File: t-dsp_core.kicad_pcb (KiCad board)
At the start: 4 copper layers, 100 x 61 mm, 164 parts, among them IC1 Logic Level Shifter - 74HCT2G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, J1 J_PWR, J10 J_DMX, J11 J_LED, J12 J_ETH, J13 u.FL DNP (IDC767 ext-antenna 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, J2 J_TDM, J3 J_T, J4 J_USBH, J5 J_MIDI, J6 J_SPDIF, J7 J_AUX, J8 J_S3, T108 Tab, T109 Tab, T110 Tab, T111 Tab, U1 Teensy 4.1 - DEVKIT, U11 Dual Buffer - SN74LVC2G125DCTR, U13 ESP32-S3-WROOM-1-N16R8, U15 LT3045EMSE#TRPBF, U16 THVD1450DR, U17 ISO7762DW, U18 TEA1-0505HI, U19 SRC4382IPFBR, U20 TLV75718PDRVR, U21 74LVC157APW, U22 IDC777-1, U23 74LVC157APW, U24 AP63203WU, U3 Power Mux & Protect - TPS2116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, U4 Optoisolators - H11L1SM - 6-S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, U5 Dual Buffer - SN74LVC2G125DCTR, U6 Dual Buffer - SN74LVC2G125DCTR, U7 Dual Buffer - SN74LVC2G125DCTR, U8 Dual Buffer - SN74LVC2G125DCTR, U9 Dual Buffer - 74HCT2G17GW,125, Y1 24.576MHz

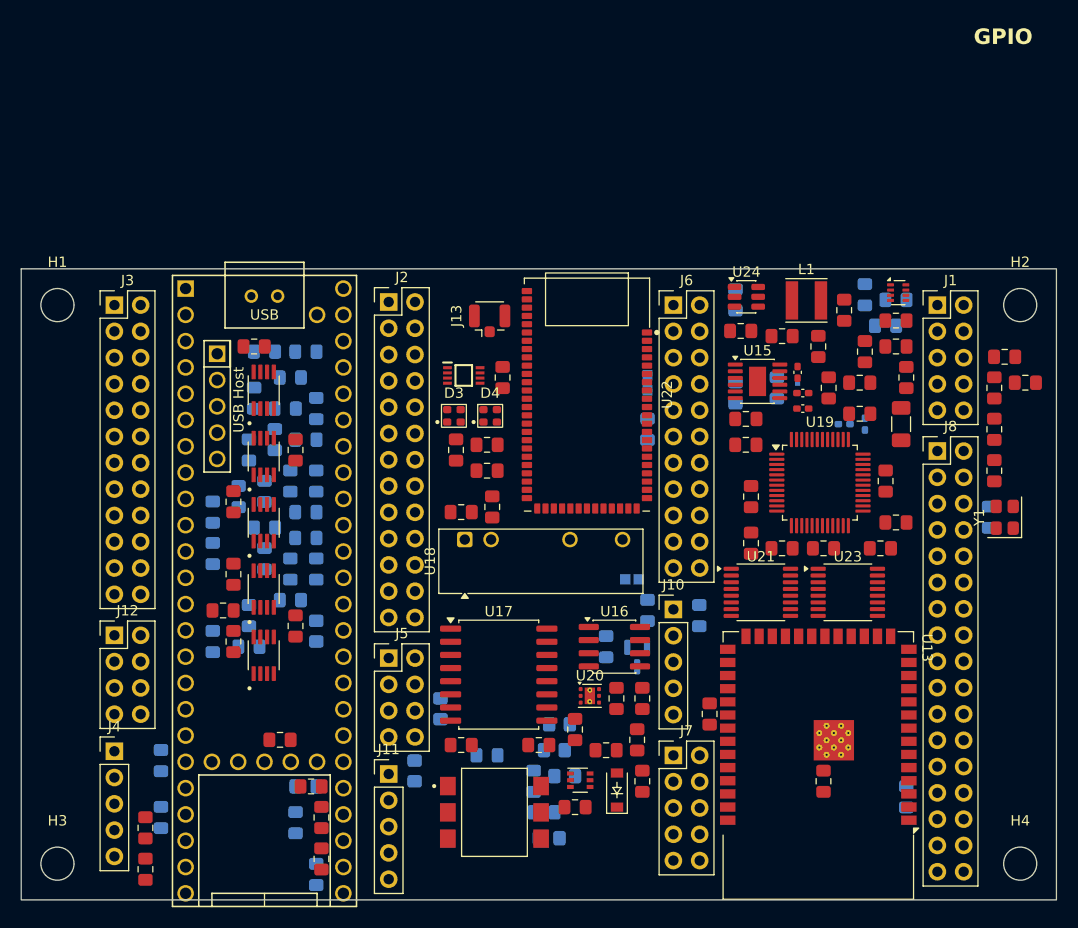
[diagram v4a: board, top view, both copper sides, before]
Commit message: Spin 2 stage 10n: outer header rows at the board edges between the corner holes (J3/J12 left, J8 right; J4 to row B, J1 to row C, J10/J11 into slot 2); 0805 passives to 0603 JLC basic parts (51 caps, 52 resistors, LCSC fields updated, 2.21k -> 2.2k); board footprints/values/fields synced via pcbnew; passives re-placed two-sided
Passive-to-pin median 2.2 mm (was 9.9 at stage 10l), 6 of 118 > 10 mm. DRC: only the stock ESP32
courtyard overlaps and inherited drill warnings; schematic parity clean apart from the board_outline2
footprint that has never had a symbol.

Co-Authored-By: Claude Fable 5.1 <noreply@anthropic.com>
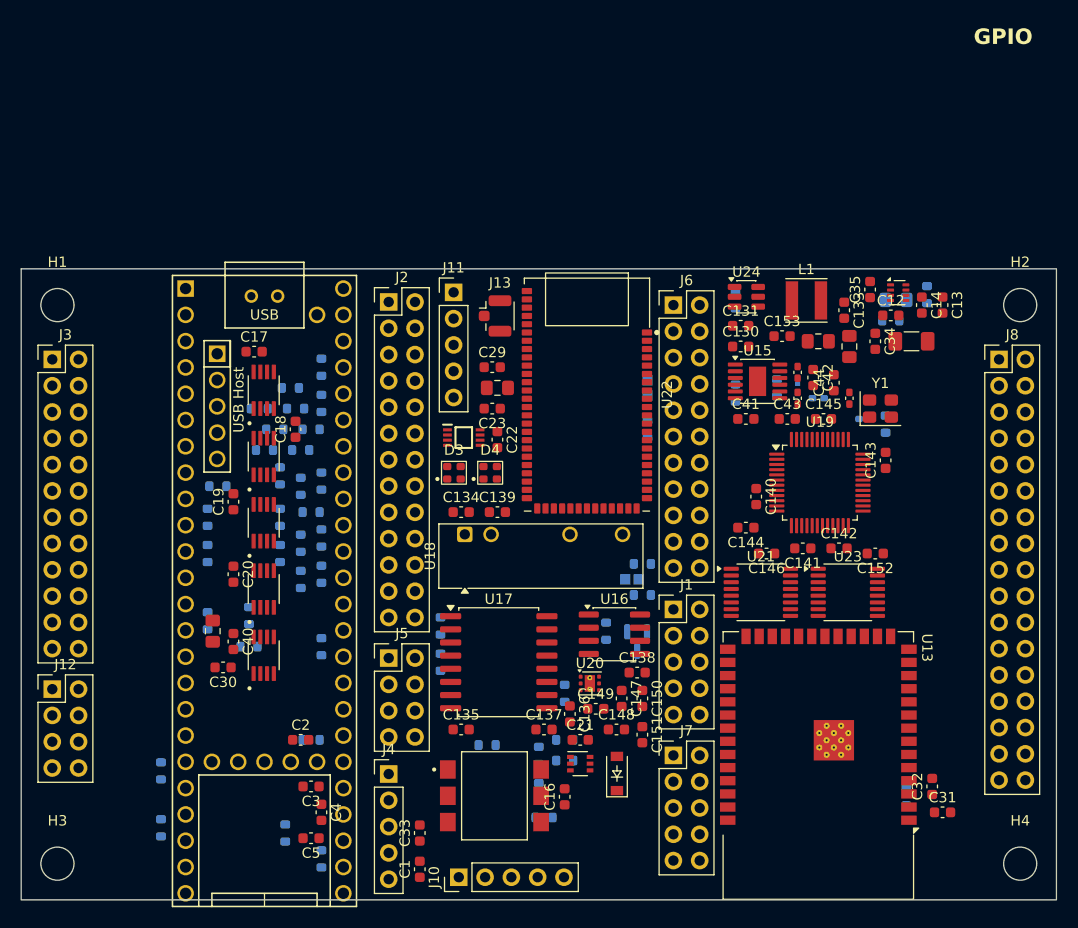
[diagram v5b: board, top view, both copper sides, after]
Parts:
- C1, C12, C13, C130, C131, C133, C134, C135, C136, C137, C138, C139, C14, C140, C141, C142, C143, C144, C145, C146, C147, C148, C149, C150, C151, C152, C153, C16, C17, C18, C19, C2, C20, C21, C22, C23, C29, C3, C30, C31, C32, C33, C34, C35, C4, C40, C41, C42, C43, C44, C5: footprint project_fp:C_0805_2012Metric_Pad1.15x1.40mm_HandSolder -> Capacitor_SMD:C_0603_1608Metric
- R1, R10, R11, R12, R15, R19, R2, R29, R3, R30, R31, R33, R35, R4, R40, R41, R42, R43, R44, R45, R46, R47, R5, R52, R53, R54, R55, R56, R57, R58, R6, R61, R66, R7, R71, R72, R73, R9: footprint project_fp:R_0805_2012Metric_Pad1.15x1.40mm_HandSolder -> Resistor_SMD:R_0603_1608Metric
- R13, R14, R16, R17, R67, R68: value 2.21k ohm -> 2.2k ohm; footprint project_fp:R_0805_2012Metric_Pad1.15x1.40mm_HandSolder -> Resistor_SMD:R_0603_1608Metric
- R32, R34, R36, R37, R38, R39, R8: footprint project_fp:R_0805_2012Metric_Pad1.20x1.40mm_HandSolder -> Resistor_SMD:R_0603_1608Metric
- moved C151 50.6 mm to (160.0, 184.0), turned to -90 degrees
- moved J11 47.0 mm to (141.8, 141.3)
- moved C150 45.3 mm to (160.0, 180.5)
- moved J1 38.9 mm to (163.0, 171.9)
- moved J10 33.2 mm to (142.3, 197.8), turned to 90 degrees
- moved J4 26.6 mm to (135.5, 187.8)
- moved C33 26.5 mm to (138.5, 193.5)
- moved C1 26.5 mm to (138.5, 197.0), turned to 90 degrees
- moved C31 24.4 mm to (189.0, 191.5), turned to 0 degrees
- moved C134 22.5 mm to (142.5, 162.5)
- moved C135 21.0 mm to (142.5, 183.5)
- moved C43 20.0 mm to (174.0, 153.5), turned to 0 degrees
- moved C44 17.7 mm to (178.5, 150.0), turned to 90 degrees
- moved Y1 15.9 mm to (183.0, 152.5), turned to 0 degrees
- moved C34 15.0 mm to (182.5, 146.0), turned to -90 degrees
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
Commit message: Spin 2 stage 10o: Teensy in the middle slot, MIDI + DMX top right, SRC4382 + muxes and IDC777 in the left slot (antenna down), power top left under a horizontal J1; header rows re-dealt (A J6/J7, B J3/J4/J11, C J5/J2/J12, D J8, J10 horizontal top right); passives re-placed two-sided
Co-Authored-By: Claude Fable 5.1 <noreply@anthropic.com>
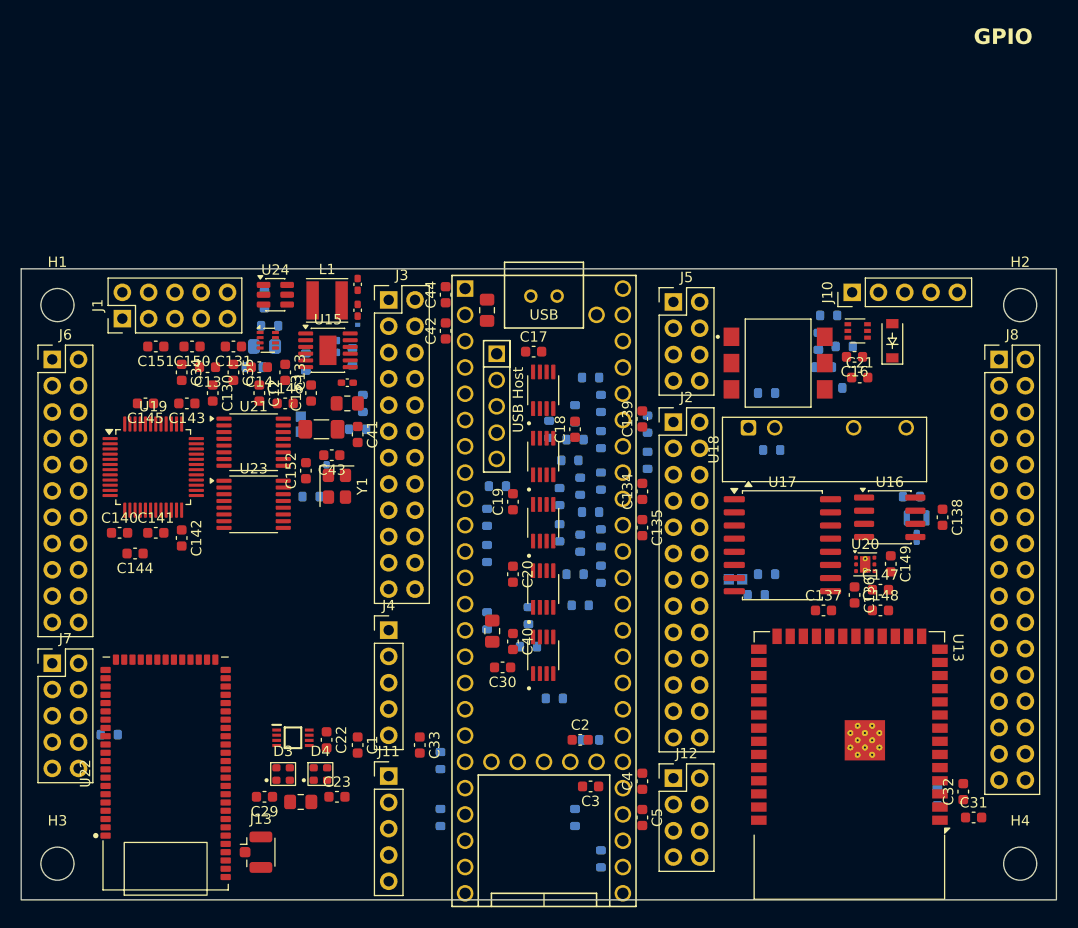
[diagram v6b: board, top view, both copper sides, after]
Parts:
- moved C13 71.3 mm to (118.0, 148.5), turned to 180 degrees
- moved J10 68.1 mm to (180.3, 141.3)
- moved C143 67.7 mm to (116.0, 152.0), turned to 180 degrees
- moved C34 67.1 mm to (115.5, 149.0)
- moved C145 65.5 mm to (112.0, 152.0), turned to 180 degrees
- moved U19 64.4 mm to (112.8, 158.2)
- moved C14 64.3 mm to (123.0, 148.5), turned to 180 degrees
- moved R30 63.6 mm to (124.0, 144.5), turned to 180 degrees
- moved C142 63.5 mm to (115.5, 165.0), turned to -90 degrees
- moved C141 62.5 mm to (113.0, 164.5), turned to 0 degrees
- moved C35 62.0 mm to (120.5, 149.0), turned to -90 degrees
- moved R29 61.7 mm to (122.5, 148.5), turned to 0 degrees
- moved C140 61.6 mm to (109.5, 164.5), turned to 0 degrees
- moved C12 61.5 mm to (123.0, 151.0), turned to -90 degrees
- moved R28 61.2 mm to (123.5, 146.5)
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
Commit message: Spin 2 stage 10p: SRC4382 under the Teensy below its interior pad row; muxes to the left column; passives re-placed
Co-Authored-By: Claude Fable 5.1 <noreply@anthropic.com>
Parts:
- moved C143 58.8 mm to (160.0, 191.0), turned to 90 degrees
- moved C142 54.5 mm to (160.0, 196.5), turned to 90 degrees
- moved U19 51.4 mm to (150.4, 193.2)
- moved C145 50.4 mm to (150.5, 184.5)
- moved C141 43.7 mm to (141.0, 198.0), turned to -90 degrees
- moved C140 42.8 mm to (141.0, 193.5), turned to 90 degrees
- moved C144 41.0 mm to (139.0, 196.5), turned to 90 degrees
- moved C154 19.6 mm to (128.5, 153.5)
- moved R2 16.0 mm to (146.0, 163.0), turned to 0 degrees
- moved R61 15.6 mm to (138.5, 172.5), turned to 0 degrees
- moved R1 14.7 mm to (145.0, 160.5)
- moved C146 11.0 mm to (114.5, 152.0)
- moved C152 11.0 mm to (116.5, 158.5)
- moved U21 11.0 mm to (111.5, 155.8)
- moved U23 11.0 mm to (111.5, 161.8)
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
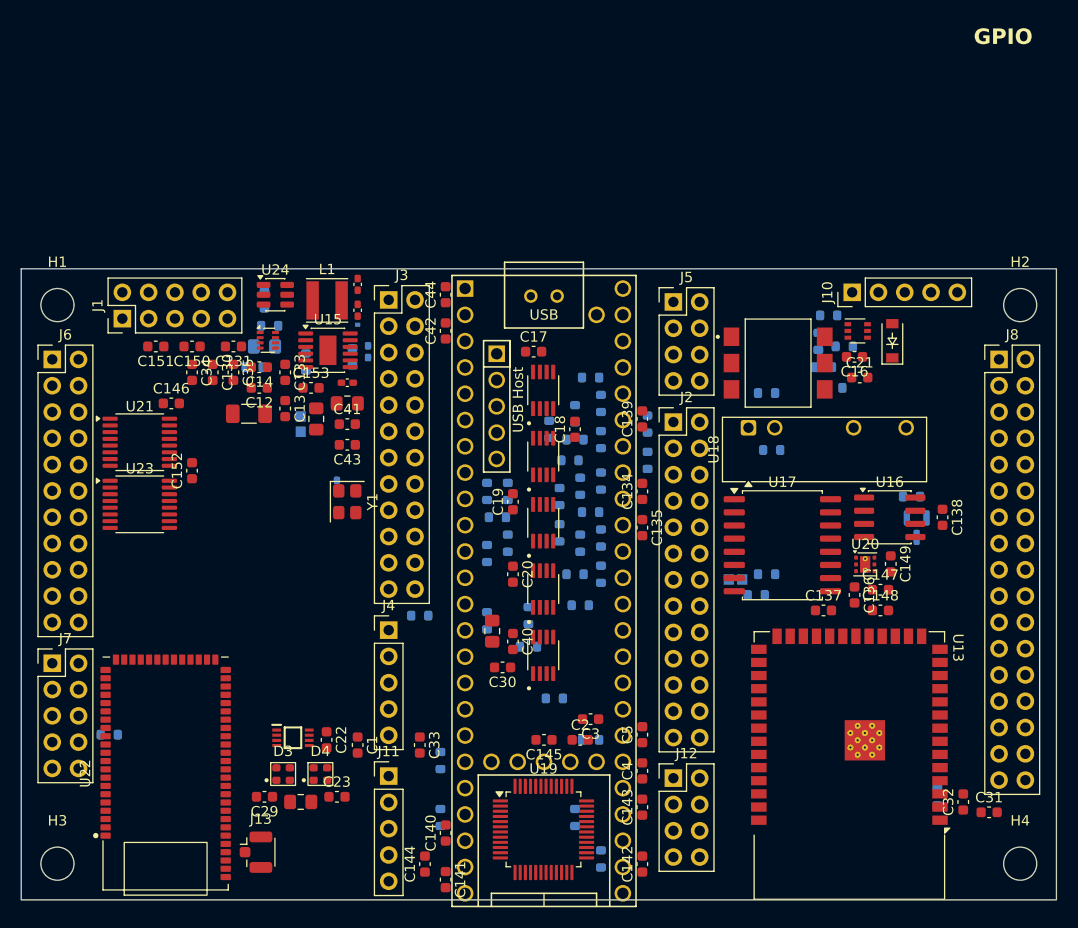
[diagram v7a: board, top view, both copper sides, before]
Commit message: Spin 2 stage 10q: muxes U21/U23 under the Teensy beside the SRC4382, TDM buffers tightened; passives re-placed
Co-Authored-By: Claude Fable 5.1 <noreply@anthropic.com>
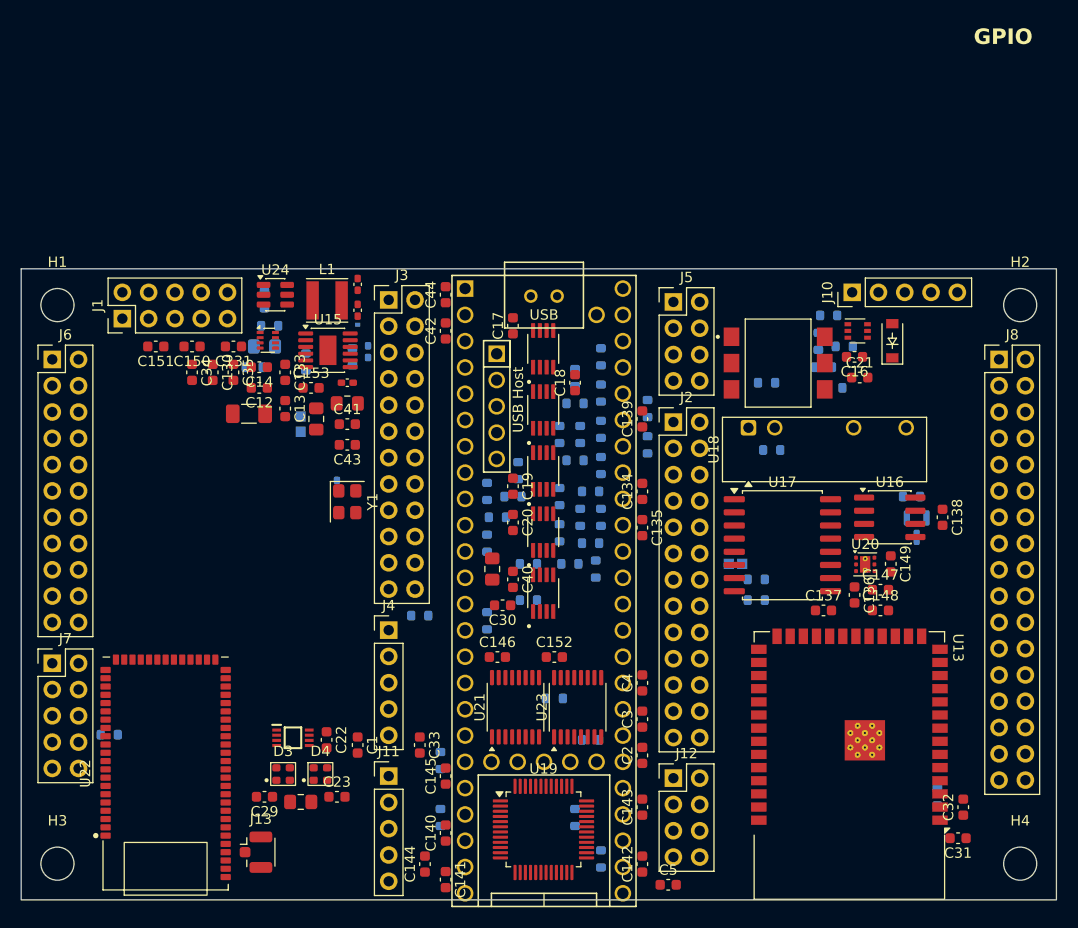
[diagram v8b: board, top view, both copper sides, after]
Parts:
- moved U23 46.6 mm to (153.8, 181.4), turned to 90 degrees
- moved U21 44.4 mm to (147.8, 181.4), turned to 90 degrees
- moved C146 39.9 mm to (146.0, 176.5)
- moved C152 39.4 mm to (151.5, 176.5), turned to 0 degrees
- moved C5 14.7 mm to (162.5, 198.5), turned to 0 degrees
- moved C145 10.1 mm to (141.0, 188.0), turned to 90 degrees
- moved C4 8.50 mm to (160.0, 179.0)
- moved C2 6.18 mm to (160.0, 186.0), turned to 90 degrees
- moved R43 6.10 mm to (156.0, 151.0)
- moved C27 6.00 mm to (145.5, 168.0)
- moved C30 6.00 mm to (146.5, 171.5)
- moved C40 6.00 mm to (147.5, 169.0)
- moved U11 6.00 mm to (150.4, 170.4)
- moved R17 5.66 mm to (152.0, 164.5)
- moved U8 5.50 mm to (150.4, 164.5)
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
